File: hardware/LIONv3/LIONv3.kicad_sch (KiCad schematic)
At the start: 41 parts, among them SW1 RESET, SW2 BOOT, U1 HC-1_25-2PWT, U2 HC-1_25-2PWT, U3 ESP32-C6-MINI-1-N4, U5 HC-1_25-2PWT, U6 TMP112AIDRLR, U7 USBLC6-2SC6, U8 TYPE-C_16PIN_2MD(073)

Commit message: refactor(hardware): improve schematic
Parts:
- C7: LCSC (none) -> C307331

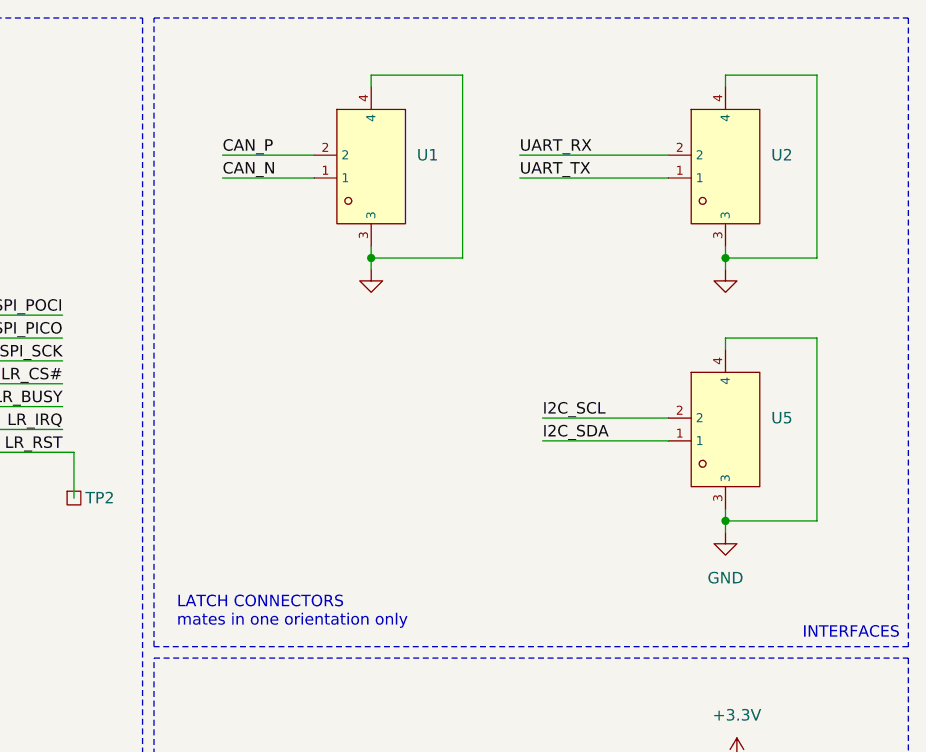
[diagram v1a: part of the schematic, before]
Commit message: feat(hardware): improve silkscreen positioning
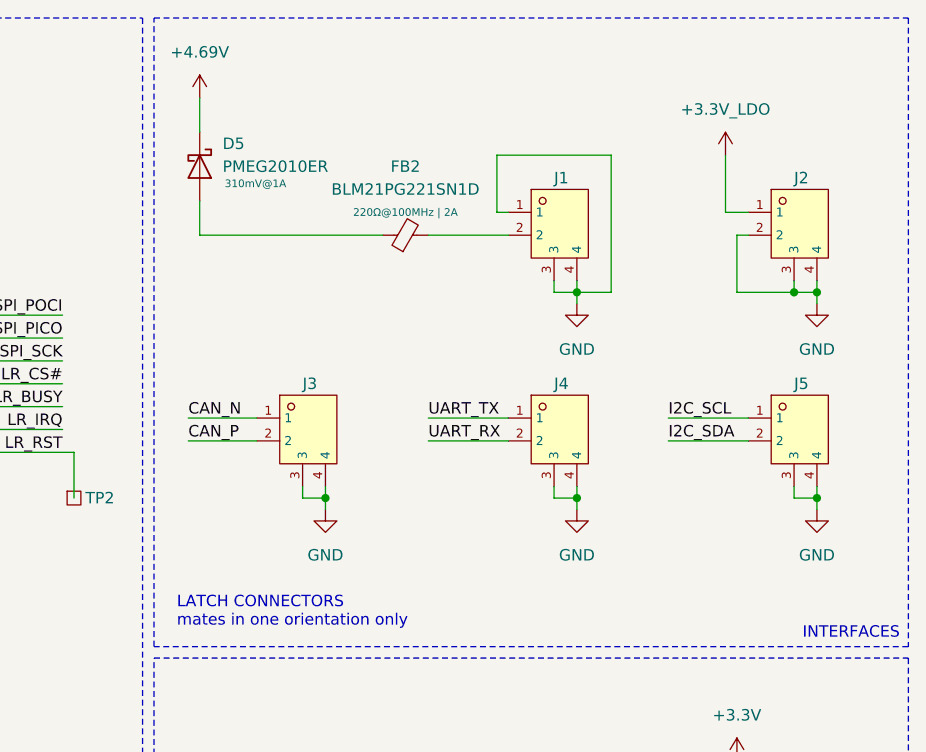
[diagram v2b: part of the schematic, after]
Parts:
- removed U1, U2, U5: HC-1_25-2PWT, LIONv3-Footprints:CONN-SMD_2P-P1.25-HC-1.25-2PWT, symbol LIONv3-Symbols:HC-1_25-2PWT
- added D5: PMEG2010ER, Diode_SMD:Nexperia_CFP3_SOD-123W, symbol Diode:PMEG2010ER
- added FB2: BLM21PG221SN1D, Inductor_SMD:L_0805_2012Metric, symbol Device:FerriteBead_Small
- added J1, J2, J3, J4, J5: 532610271, LIONv3-Footprints:CONN-SMD_532610271, symbol LIONv3-Symbols:532610271_C177225
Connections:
- net +4.69V: now also D5.1 (K)
- net CAN_N: now also J3.1
- net CAN_P: now also J3.2
- net GND: now also J1.1, J1.3, J1.4, J2.2, J2.3, J2.4, J3.3, J3.4, J4.3, J4.4, J5.3, J5.4
- net I2C_SCL: now also J5.1
- net I2C_SDA: now also J5.2
- net UART_RX: now also J4.2
- net UART_TX: now also J4.1
- new net: FB2.2, J1.2
- new net: D5.2 (A), FB2.1
- new net +3.3V_LDO: J2.1

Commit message: feat(hardware): finish LIONv3-Mini routing
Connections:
- net I2C_SCL: now also J5.2; no longer J5.1
- net I2C_SDA: now also J5.1; no longer J5.2
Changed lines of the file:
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@@
+		)
+	)
+	(label "I2C_SCL"
+		(at 256.54 60.96 0)
+		(effects
+			(font
+				(size 1.27 1.27)
+			)
+			(justify left bottom)
 		)
 	)
@@
 		)
 	)
-	(label "I2C_SCL"
-		(at 256.54 58.42 0)
-		(effects
-			(font
-				(size 1.27 1.27)
-			)
-			(justify left bottom)
-		)
-	)
 	(label "CAN_N"
 		(at 45.72 116.84 180)
@@
 		)
 	)
+	(label "I2C_SDA"
+		(at 256.54 58.42 0)
+		(effects
+			(font
+				(size 1.27 1.27)
+			)
+			(justify left bottom)
+		)
+	)
 	(label "INA_ALERT"
 		(at 45.72 99.06 180)
@@
 		(effects
 			(font
-				(size 1.27 1.27)
-			)
-			(justify left bottom)
-		)
-	)
-	(label "I2C_SDA"
-		(at 256.54 60.96 0)
-		(effects
-			(font

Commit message: feat(hardware): finish LIONv3-Mini rev1.0
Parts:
- removed J1, J2, J3, J4, J5: 532610271, LIONv3-Footprints:CONN-SMD_532610271, symbol LIONv3-Symbols:532610271_C177225
- removed TP1, TP2, TP3, TP4, TP5, TP6, TP7: TestPoint_Square, TestPoint:TestPoint_Pad_D1.5mm, symbol Connector:TestPoint_Square
- added J1, J2, J3, J4, J5: 532610271, LIONv3-Footprints:Molex_PicoBlade_53261-0271_1x02-1MP_P1.25mm_Horizontal, symbol Connector_Generic:Conn_01x04
- SW1: value RESET -> (none)
- SW2: value BOOT -> (none)
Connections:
- net +3.3V_LDO: now also J2.1 (Pin_1)
- net CAN_N: now also J3.1 (Pin_1)
- net CAN_P: now also J3.2 (Pin_2)
- net GND: now also J1.1 (Pin_1), J1.3 (Pin_3), J1.4 (Pin_4), J2.2 (Pin_2), J2.3 (Pin_3), J2.4 (Pin_4), J3.3 (Pin_3), J3.4 (Pin_4), J4.3 (Pin_3), J4.4 (Pin_4), J5.3 (Pin_3), J5.4 (Pin_4)
- net I2C_SCL: now also J5.2 (Pin_2)
- net I2C_SDA: now also J5.1 (Pin_1)
- net UART_RX: now also J4.2 (Pin_2)
- net UART_TX: now also J4.1 (Pin_1)
- net at FB2.2: now also J1.2 (Pin_2)
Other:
- added sheet Block Diagram (Block Diagram.kicad_sch)
- note added: "BOOT"
- note added: "MOLEX PICOBLADE CONNECTORS mates in one orientation only"
- note added: "RESET"
- note removed: "LATCH CONNECTORS mates in one orientation only"
- moved on the sheet: D5, FB2

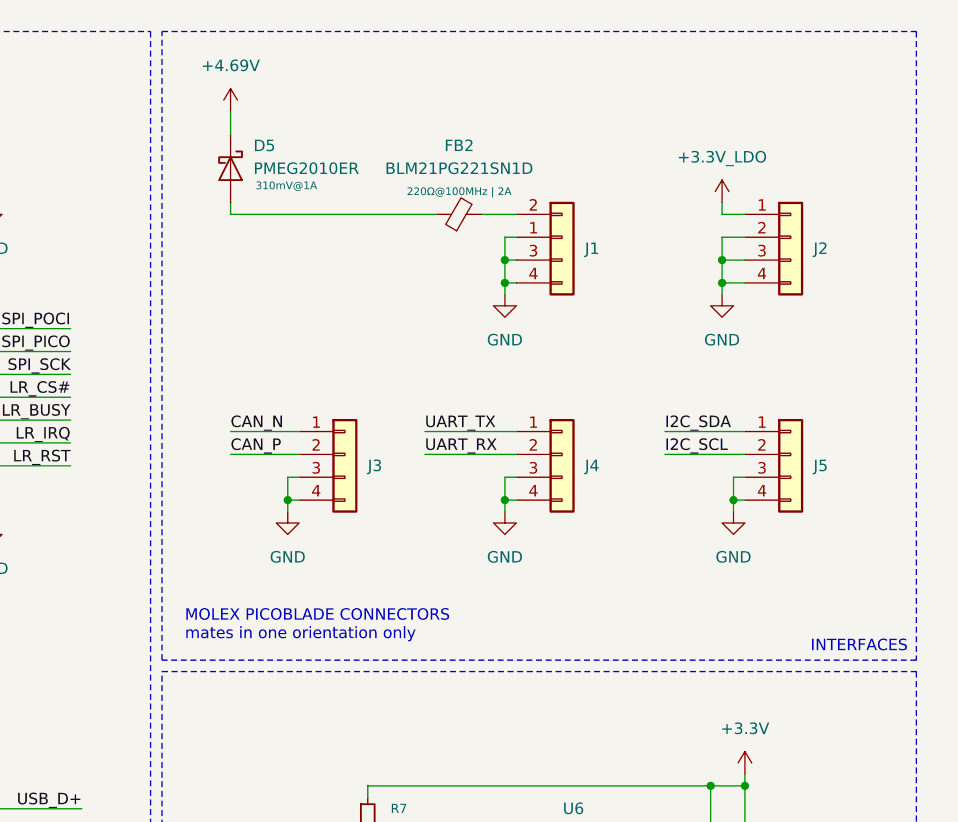
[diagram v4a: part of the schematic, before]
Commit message: refactor(hardware): improve J1-J5 connectors readability
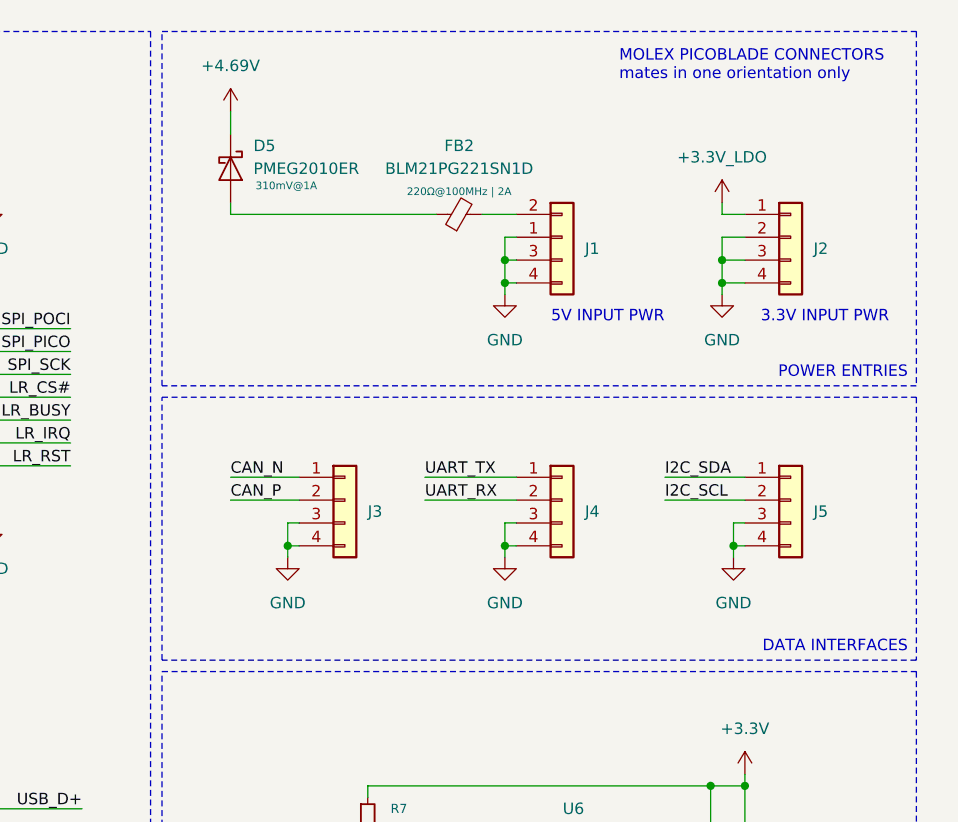
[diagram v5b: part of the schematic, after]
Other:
- note added: "3.3V INPUT PWR"
- note added: "5V INPUT PWR"
- moved on the sheet: J3, J4, J5
